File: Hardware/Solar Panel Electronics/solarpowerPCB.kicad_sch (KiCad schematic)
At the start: 39 parts

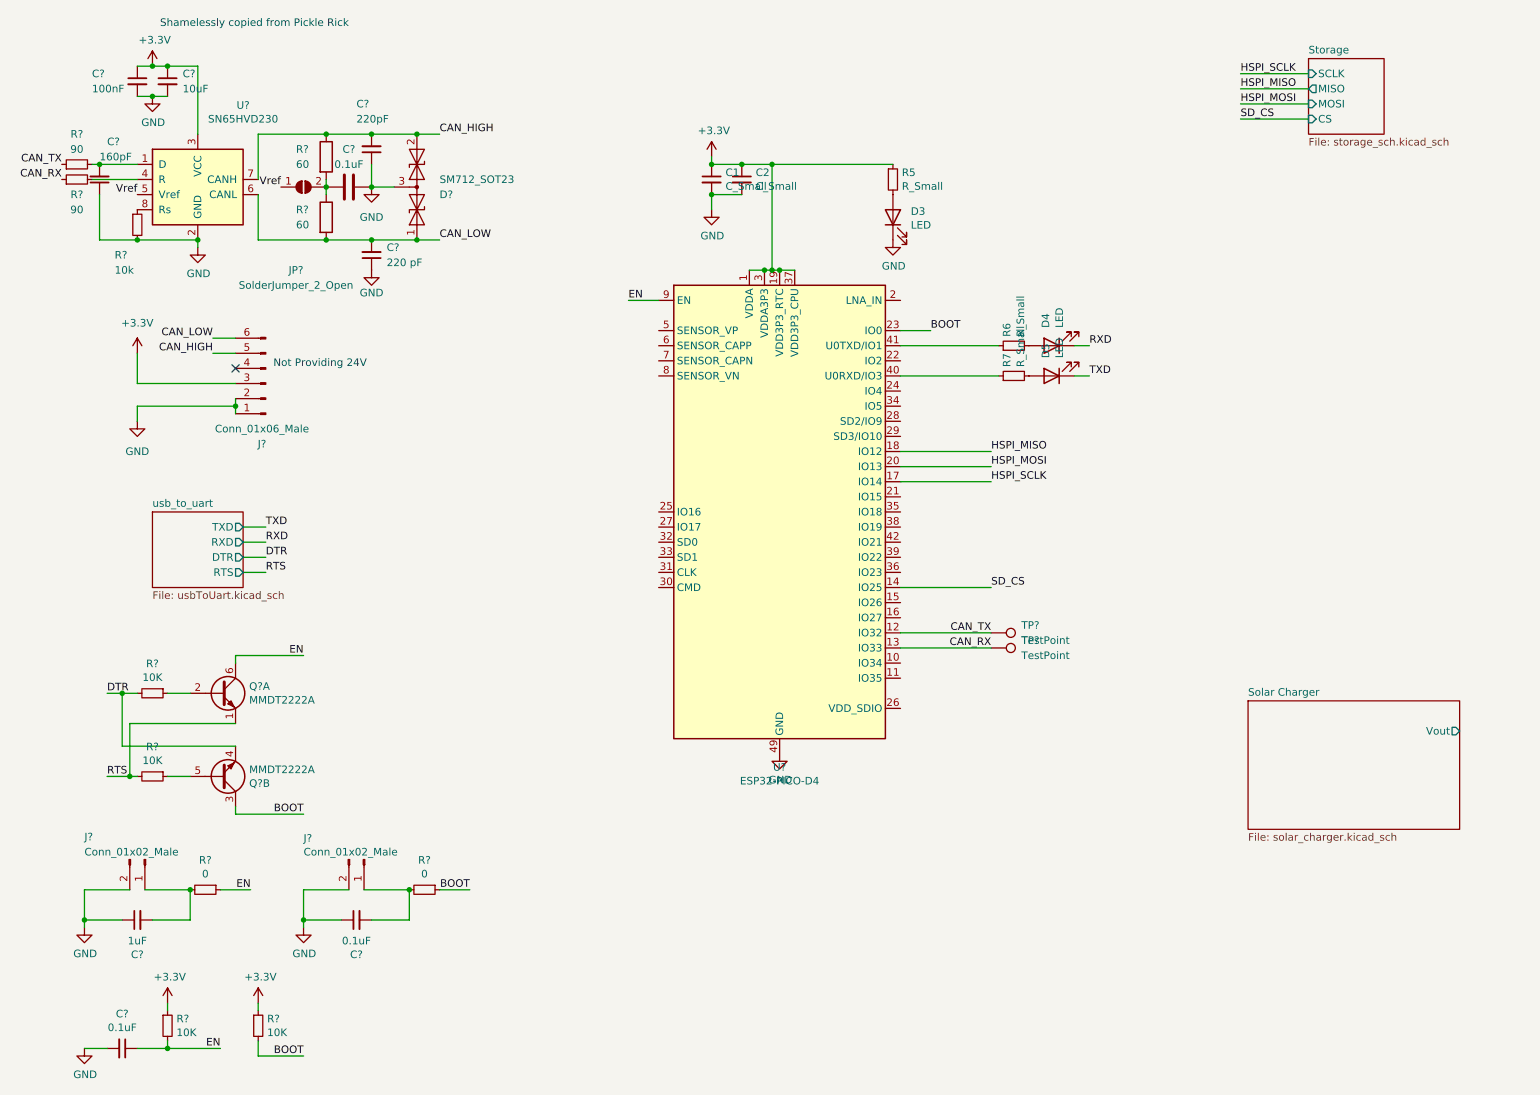
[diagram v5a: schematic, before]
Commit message: Components sized for our requirements. Added ideal diode IC LTC4411 which is more efficient than a normal diode.
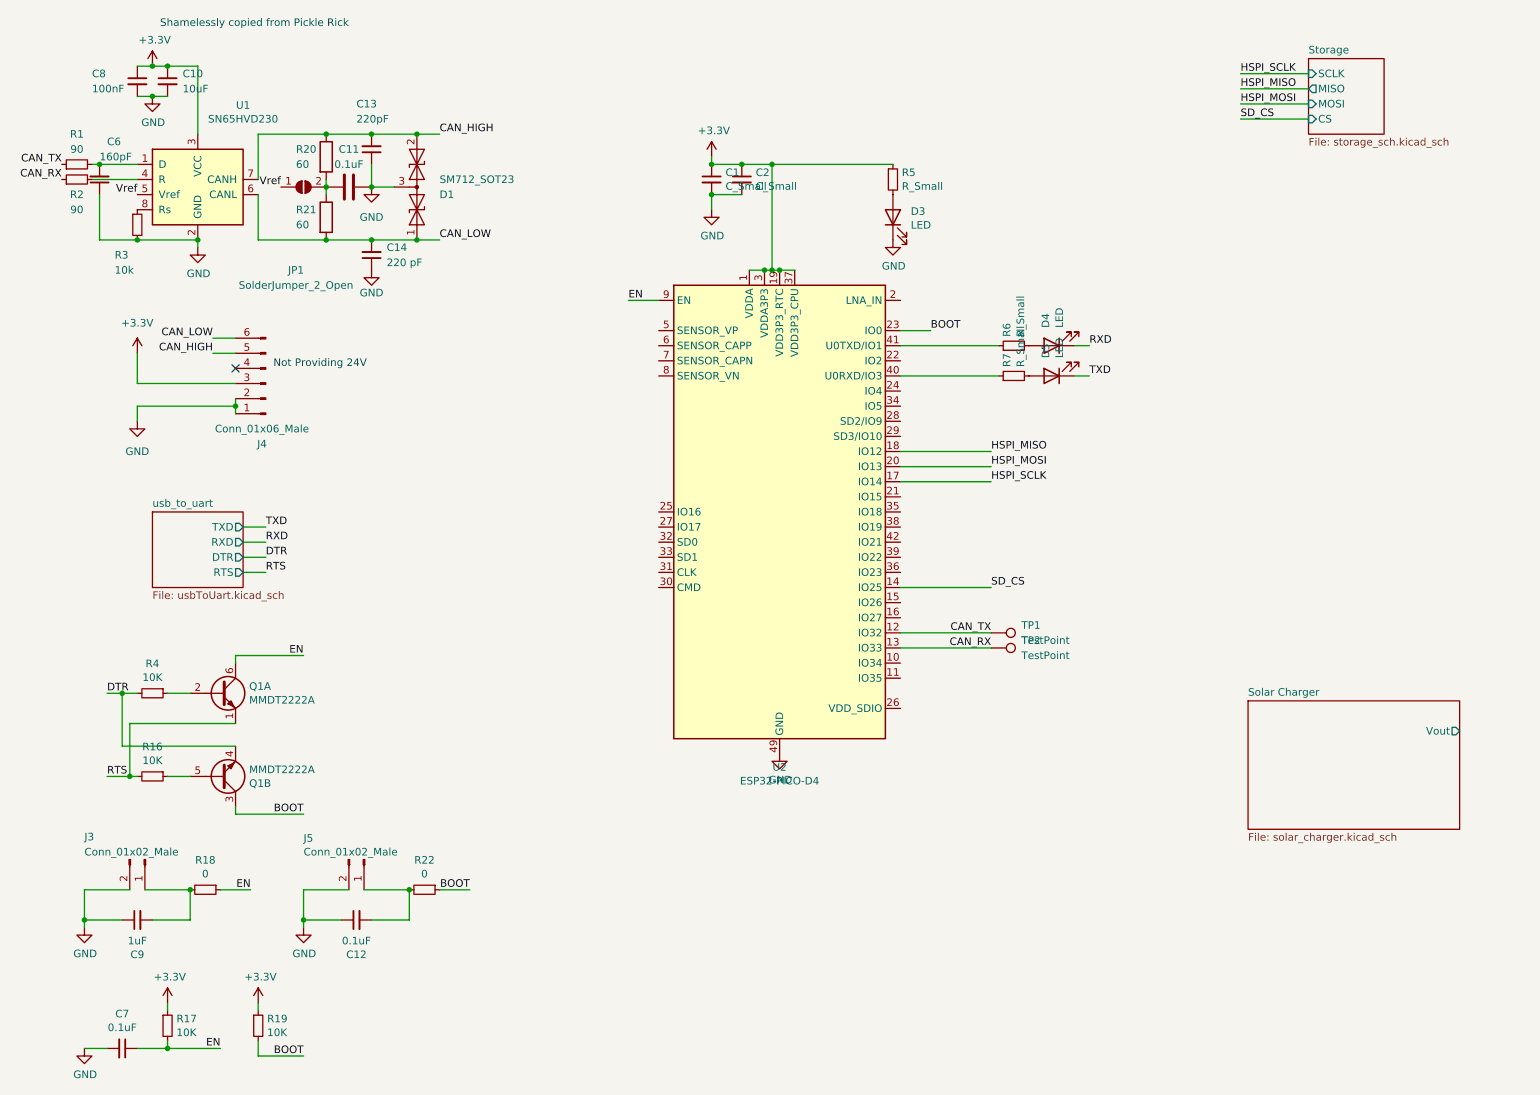
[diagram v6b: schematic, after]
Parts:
- gave numbers to parts that had none: 30

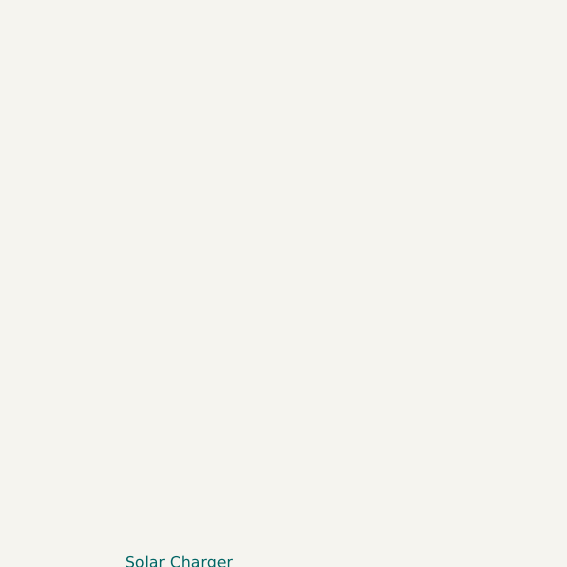
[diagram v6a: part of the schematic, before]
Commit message: Added voltage regulator from Pick Rick
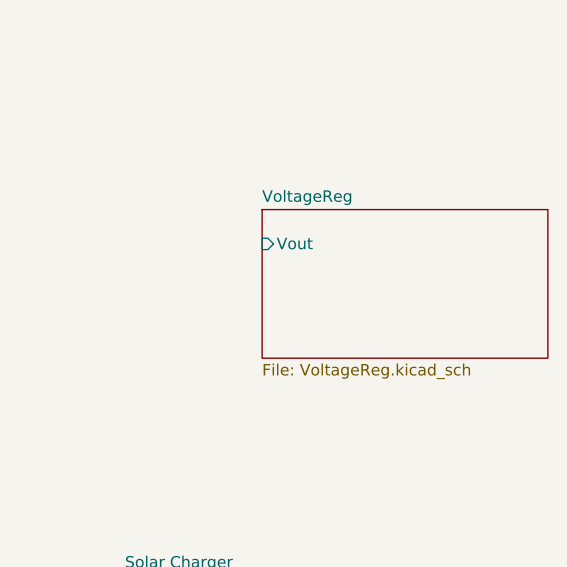
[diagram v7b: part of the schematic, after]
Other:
- added sheet VoltageReg (VoltageReg.kicad_sch)
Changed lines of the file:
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@@
+    )
+  )
+  (sheet (at 234.95 88.9) (size 31.75 16.51) (fields_autoplaced)
+    (stroke (width 0.1524) (type solid) (color 0 0 0 0))
+    (fill (color 0 0 0 0.0000))
+    (property "Sheet name" "VoltageReg" (id 0) (at 234.95 88.1884 0)
+      (effects (font (size 1.27 1.27)) (justify left bottom))
+    )
+    (property "Sheet file" "VoltageReg.kicad_sch" (id 1) (at 234.95 105.9946 0)
+      (effects (font (size 1.27 1.27)) (justify left top))
+    )
+    (pin "Vout" input (at 234.95 92.71 180)
+      (effects (font (size 1.27 1.27)) (justify left))
     )
   )
@@
     (path "/761ca562-7e61-4873-a476-3f17aaa1ae77" (page "3"))
     (path "/1cf3aab9-4829-448a-a3c1-5a595217a91d" (page "4"))
+    (path "/bc16b27f-da78-4399-84ff-d0e67df4623d" (page "5"))
   )
   (symbol_instances
@@
       (reference "#PWR0150") (unit 1) (value "GND") (footprint "")
     )
+    (path "/bc16b27f-da78-4399-84ff-d0e67df4623d/471eb4c1-1fb6-4731-b769-cc81195874cc"
+      (reference "#PWR?") (unit 1) (value "GND") (footprint "")
+    )
+    (path "/bc16b27f-da78-4399-84ff-d0e67df4623d/756c57ca-b724-416e-bbc3-080fcadffb70"
+      (reference "#PWR?") (unit 1) (value "GND") (footprint "")
+    )
+    (path "/bc16b27f-da78-4399-84ff-d0e67df4623d/b0d1f2d1-6661-413f-b789-5e4612cfd11c"
+      (reference "#PWR?") (unit 1) (value "+3V3") (footprint "")
+    )
+    (path "/bc16b27f-da78-4399-84ff-d0e67df4623d/ce052e62-9895-4eaf-b763-02bb1f2f2fc0"
+      (reference "#PWR?") (unit 1) (value "GND") (footprint "")
+    )
     (path "/00000000-0000-0000-0000-0000620b2ec1"
       (reference "C1") (unit 1) (value "C_Small") (footprint "")
@@
       (reference "C20") (unit 1) (value "10uF") (footprint "")
     )
+    (path "/bc16b27f-da78-4399-84ff-d0e67df4623d/53eb5fc0-41cc-43ad-8003-3a7163adca82"
+      (reference "C?") (unit 1) (value "10uF") (footprint "Capacitor_SMD:C_0603_1608Metric")
+    )
+    (path "/bc16b27f-da78-4399-84ff-d0e67df4623d/b54d57a7-95c9-46b9-bf84-99ca3de4bc2a"
+      (reference "C?") (unit 1) (value "10uF") (footprint "Capacitor_SMD:C_0603_1608Metric")
+    )
+    (path "/bc16b27f-da78-4399-84ff-d0e67df4623d/e4c50208-faff-4dc6-92f3-177bc479ae49"
+      (reference "C?") (unit 1) (value "100nF") (footprint "Capacitor_SMD:C_0603_1608Metric")
+    )
     (path "/0b74af2e-d916-4a23-ae3b-0ce9a9c64af1"
       (reference "D1") (unit 1) (value "SM712_SOT23") (footprint "Package_TO_SOT_SMD:SOT-23")
@@
       (reference "U5") (unit 1) (value "INTERFACE-CP2102-GMR(QFN28)") (footprint "iclr:QFN28G_0.5-5X5MM")
     )
+    (path "/bc16b27f-da78-4399-84ff-d0e67df4623d/ec7425db-97df-4e3f-a1d9-7fa3fa52762c"
+      (reference "U?") (unit 1) (value "LT1963AxST-3.3") (footprint "Package_TO_SOT_SMD:SOT-223-3_TabPin2")
+    )
   )
